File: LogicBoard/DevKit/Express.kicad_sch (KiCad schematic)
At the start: 20 parts, among them J13 USBC Socket, J15 ESPUartConn, J17 MicroSD, U10 ESP32-C3-WROOM-02-N4, U8 USBLC6-2SC6

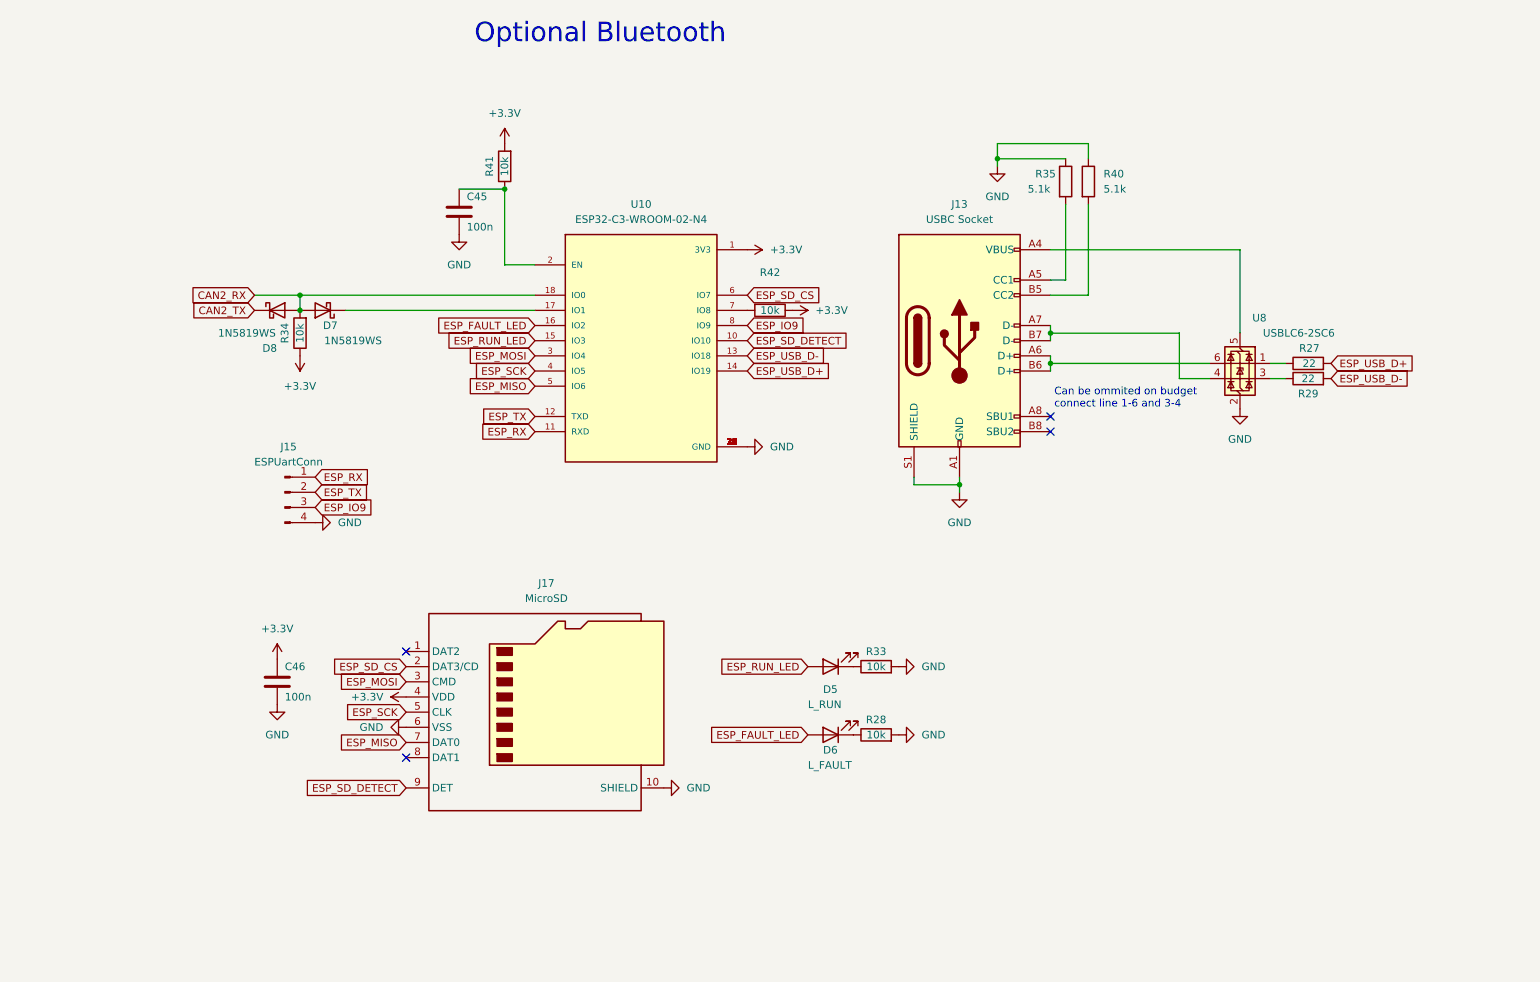
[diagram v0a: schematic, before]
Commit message: v3.3.2 - ECP2304 changes
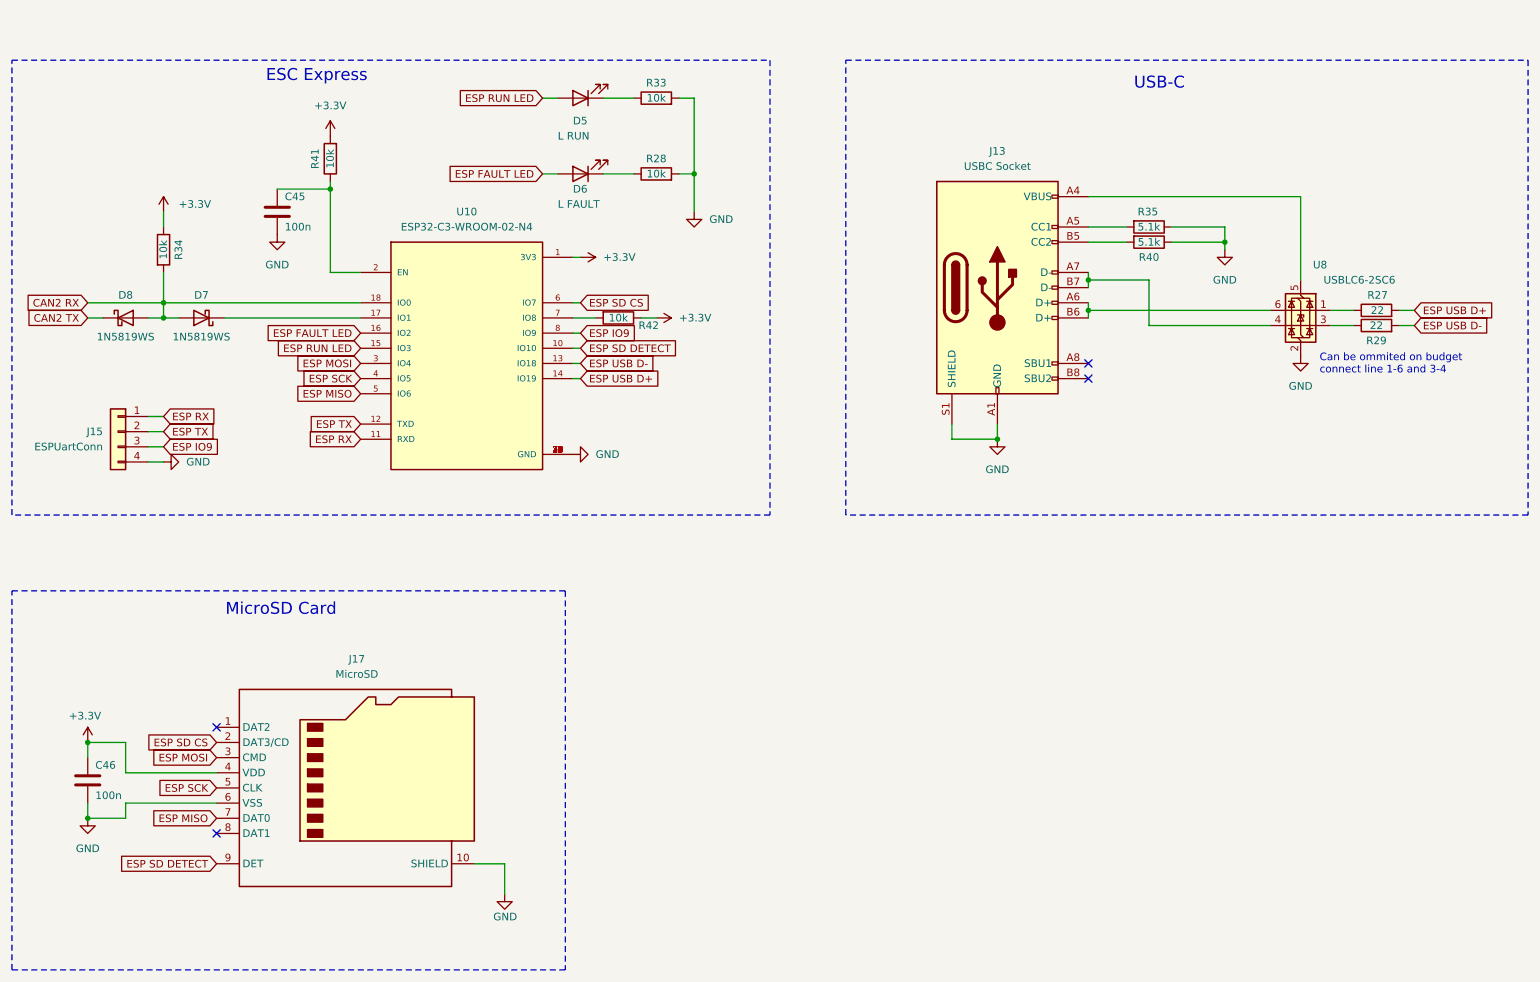
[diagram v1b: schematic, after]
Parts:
- D5: value L_RUN -> L RUN
- D6: value L_FAULT -> L FAULT
- J15: symbol Connector:Conn_01x04_Pin -> Connector_Generic:Conn_01x04; JLCPosOffset -3,0 -> 0,0
- U8: JLCRotOffset -90 -> 0
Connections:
- net CAN2_RX renamed CAN2 RX
- net CAN2_TX renamed CAN2 TX
- net ESP_FAULT_LED renamed ESP FAULT LED
- net ESP_IO9 renamed ESP IO9
- net ESP_MISO renamed ESP MISO
- net ESP_MOSI renamed ESP MOSI
- net ESP_RUN_LED renamed ESP RUN LED
- net ESP_RX renamed ESP RX
- net ESP_SCK renamed ESP SCK
- net ESP_SD_CS renamed ESP SD CS
- net ESP_SD_DETECT renamed ESP SD DETECT
- net ESP_TX renamed ESP TX
- net ESP_USB_D+ renamed ESP USB D+
- net ESP_USB_D- renamed ESP USB D-
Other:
- note added: "ESC Express"
- note added: "MicroSD Card"
- note added: "USB-C"
- note removed: "Optional Bluetooth"
- moved on the sheet: C45, C46, D5, D6, D7, D8, J13, J17, R27, R28, R29, R33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
